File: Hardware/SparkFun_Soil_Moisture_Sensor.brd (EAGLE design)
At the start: 22.9 x 61 mm, 11 parts, among them Q1 2N3904

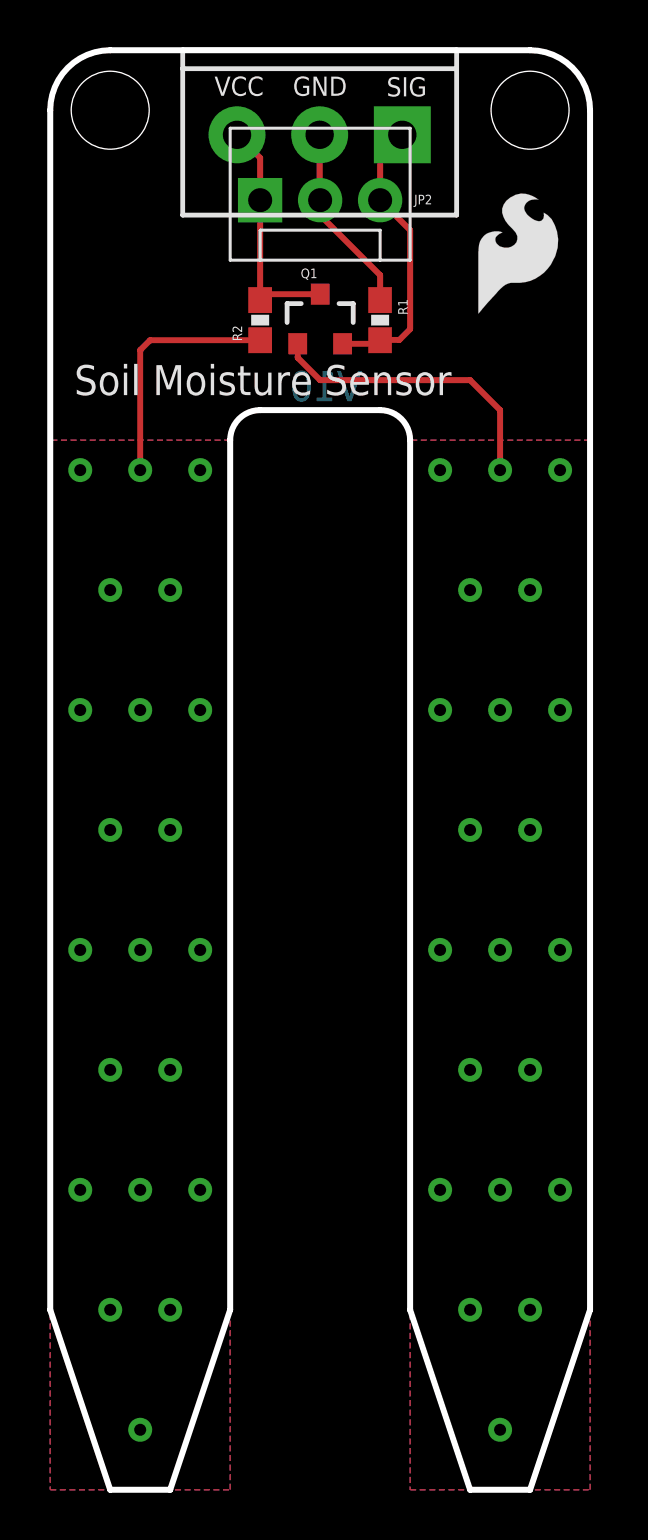
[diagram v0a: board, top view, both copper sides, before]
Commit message: Fixed QC Checklist issues
added fiducials, changed dimension width to .008, removed Ohm from
values, added Vcc range, changed version # to correct V01, corrected
dashed lines
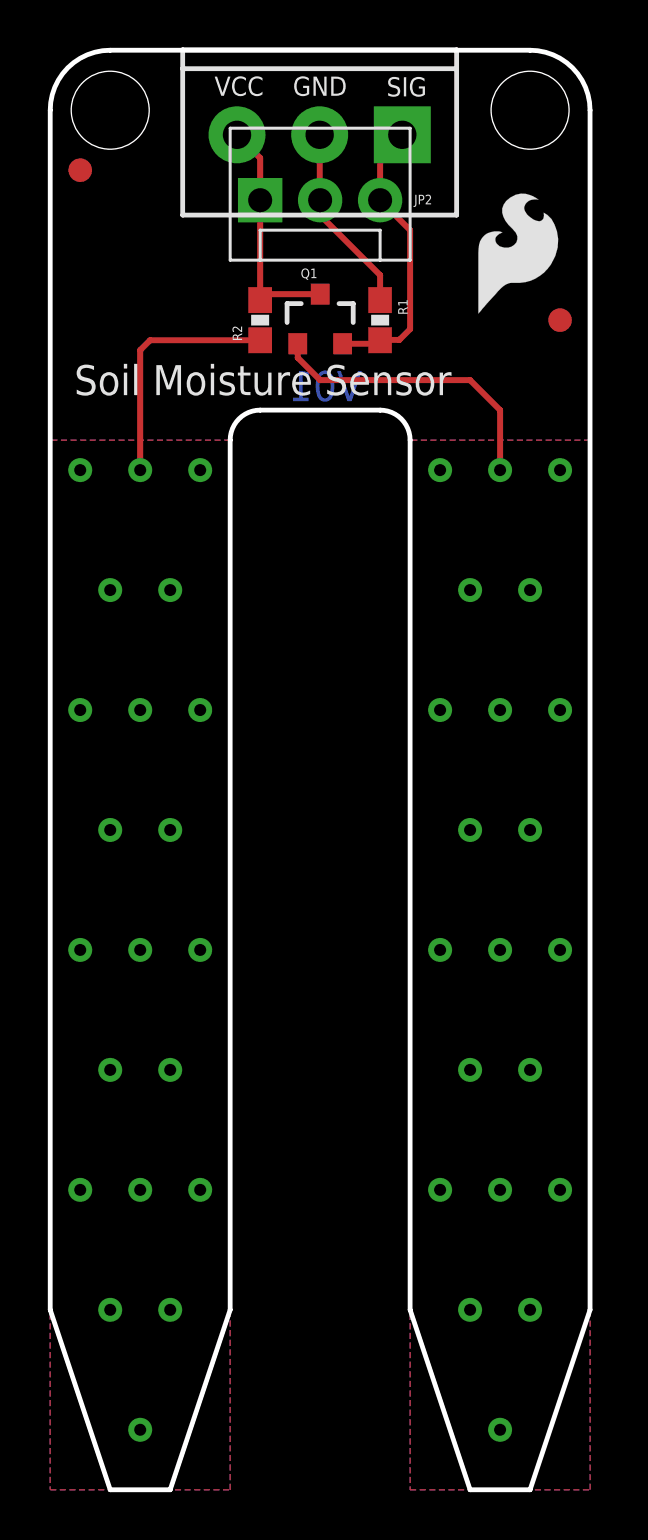
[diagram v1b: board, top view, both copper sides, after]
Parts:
- added FID1, FID2: FIDUCIAL1X2, SparkFun-Aesthetics:FIDUCIAL-1X2
- R1: value 10kOhm -> 10k
- R2: value 100Ohm -> 100
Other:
- board text added: "V01"
- board text removed: "V10"
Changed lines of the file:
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@@
 <grid distance="0.05" unitdist="inch" unit="inch" style="lines" multiple="1" display="yes" altdistance="0.005" altunitdist="inch" altunit="inch"/>
 <layers>
-<layer number="1" name="Top" color="4" fill="1" visible="no" active="yes"/>
+<layer number="1" name="Top" color="4" fill="1" visible="yes" active="yes"/>
 <layer number="2" name="Route2" color="1" fill="3" visible="no" active="no"/>
 <layer number="3" name="Route3" color="4" fill="3" visible="no" active="no"/>
@@
 <layer number="15" name="Route15" color="4" fill="6" visible="no" active="no"/>
 <layer number="16" name="Bottom" color="1" fill="1" visible="yes" active="yes"/>
-<layer number="17" name="Pads" color="2" fill="1" visible="no" active="yes"/>
-<layer number="18" name="Vias" color="2" fill="1" visible="no" active="yes"/>
-<layer number="19" name="Unrouted" color="6" fill="1" visible="no" active="yes"/>
-<layer number="20" name="Dimension" color="15" fill="1" visible="no" active="yes"/>
-<layer number="21" name="tPlace" color="16" fill="1" visible="no" active="yes"/>
-<layer number="22" name="bPlace" color="14" fill="1" visible="no" active="yes"/>
-<layer number="23" name="tOrigins" color="15" fill="1" visible="no" active="yes"/>
-<layer number="24" name="bOrigins" color="15" fill="1" visible="no" active="yes"/>
+<layer number="17" name="Pads" color="2" fill="1" visible="yes" active="yes"/>
+<layer number="18" name="Vias" color="2" fill="1" visible="yes" active="yes"/>
+<layer number="19" name="Unrouted" color="6" fill="1" visible="yes" active="yes"/>
+<layer number="20" name="Dimension" color="15" fill="1" visible="yes" active="yes"/>
+<layer number="21" name="tPlace" color="16" fill="1" visible="yes" active="yes"/>
+<layer number="22" name="bPlace" color="14" fill="1" visible="yes" active="yes"/>
+<layer number="23" name="tOrigins" color="15" fill="1" visible="yes" active="yes"/>
+<layer number="24" name="bOrigins" color="15" fill="1" visible="yes" active="yes"/>
 <layer number="25" name="tNames" color="7" fill="1" visible="no" active="yes"/>
 <layer number="26" name="bNames" color="7" fill="1" visible="no" active="yes"/>
 <layer number="27" name="tValues" color="7" fill="1" visible="no" active="yes"/>
 <layer number="28" name="bValues" color="7" fill="1" visible="no" active="yes"/>
-<layer number="29" name="tStop" color="7" fill="3" visible="yes" active="yes"/>
-<layer number="30" name="bStop" color="7" fill="6" visible="yes" active="yes"/>
+<layer number="29" name="tStop" color="7" fill="3" visible="no" active="yes"/>
+<layer number="30" name="bStop" color="7" fill="6" visible="no" active="yes"/>
 <layer number="31" name="tCream" color="7" fill="4" visible="no" active="yes"/>
 <layer number="32" name="bCream" color="7" fill="5" visible="no" active="yes"/>
@@
 <layer number="43" name="vRestrict" color="2" fill="10" visible="no" active="yes"/>
 <layer number="44" name="Drills" color="7" fill="1" visible="no" active="yes"/>
-<layer number="45" name="Holes" color="7" fill="1" visible="no" active="yes"/>
+<layer number="45" name="Holes" color="7" fill="1" visible="yes" active="yes"/>
 <layer number="46" name="Milling" color="3" fill="1" visible="no" active="yes"/>
 <layer number="47" name="Measures" color="7" fill="1" visible="no" active="yes"/>
@@
 <layer number="49" name="Reference" color="7" fill="1" visible="no" active="yes"/>
 <layer number="50" name="dxf" color="7" fill="1" visible="no" active="no"/>
-<layer number="51" name="tDocu" color="6" fill="1" visible="no" active="yes"/>
+<layer number="51" name="tDocu" color="6" fill="1" visible="yes" active="yes"/>
 <layer number="52" name="bDocu" color="7" fill="1" visible="no" active="yes"/>
 <layer number="53" name="tGND_GNDA" color="7" fill="9" visible="no" active="no"/>
@@
 <plain>
 <dimension x1="22.86" y1="60.96" x2="22.86" y2="0" x3="30.48" y3="30.48" textsize="1.778" textratio="15" layer="51" unit="inch"/>
-<wire x1="2.54" y1="60.96" x2="0" y2="58.42" width="0.254" layer="20" curve="90"/>
-<wire x1="0" y1="58.42" x2="0" y2="7.62" width="0.254" layer="20"/>
+<wire x1="2.54" y1="60.96" x2="0" y2="58.42" width="0.2032" layer="20" curve="90"/>
+<wire x1="0" y1="58.42" x2="0" y2="7.62" width="0.2032" layer="20"/>
 <dimension x1="0" y1="60.96" x2="22.86" y2="60.96" x3="11.43" y3="64.77" textsize="1.778" textratio="15" layer="51" unit="inch"/>
-<wire x1="2.54" y1="60.96" x2="20.32" y2="60.96" width="0.254" layer="20"/>
-<wire x1="20.32" y1="60.96" x2="22.86" y2="58.42" width="0.254" layer="20" curve="-90"/>
-<wire x1="22.86" y1="58.42" x2="22.86" y2="7.62" width="0.254" layer="20"/>
-<wire x1="22.86" y1="7.62" x2="20.32" y2="0" width="0.254" layer="20"/>
-<wire x1="20.32" y1="0" x2="17.78" y2="0" width="0.254" layer="20"/>
-<wire x1="17.78" y1="0" x2="15.24" y2="7.62" width="0.254" layer="20"/>
-<wire x1="0" y1="7.62" x2="2.54" y2="0" width="0.254" layer="20"/>
-<wire x1="2.54" y1="0" x2="5.08" y2="0" width="0.254" layer="20"/>
-<wire x1="5.08" y1="0" x2="7.62" y2="7.62" width="0.254" layer="20"/>
-<wire x1="7.62" y1="7.62" x2="7.62" y2="44.45" width="0.254" layer="20"/>
-<wire x1="7.62" y1="44.45" x2="8.89" y2="45.72" width="0.254" layer="20" curve="-90"/>
-<wire x1="8.89" y1="45.72" x2="13.97" y2="45.72" width="0.254" layer="20"/>
-<wire x1="15.24" y1="7.62" x2="15.24" y2="44.45" width="0.254" layer="20"/>
-<wire x1="15.24" y1="44.45" x2="13.97" y2="45.72" width="0.254" layer="20" curve="90"/>
+<wire x1="2.54" y1="60.96" x2="20.32" y2="60.96" width="0.2032" layer="20"/>
+<wire x1="20.32" y1="60.96" x2="22.86" y2="58.42" width="0.2032" layer="20" curve="-90"/>
+<wire x1="22.86" y1="58.42" x2="22.86" y2="7.62" width="0.2032" layer="20"/>
+<wire x1="22.86" y1="7.62" x2="20.32" y2="0" width="0.2032" layer="20"/>
+<wire x1="20.32" y1="0" x2="17.78" y2="0" width="0.2032" layer="20"/>
+<wire x1="17.78" y1="0" x2="15.24" y2="7.62" width="0.2032" layer="20"/>
+<wire x1="0" y1="7.62" x2="2.54" y2="0" width="0.2032" layer="20"/>
+<wire x1="2.54" y1="0" x2="5.08" y2="0" width="0.2032" layer="20"/>
+<wire x1="5.08" y1="0" x2="7.62" y2="7.62" width="0.2032" layer="20"/>
+<wire x1="7.62" y1="7.62" x2="7.62" y2="44.45" width="0.2032" layer="20"/>
+<wire x1="7.62" y1="44.45" x2="8.89" y2="45.72" width="0.2032" layer="20" curve="-90"/>
+<wire x1="8.89" y1="45.72" x2="13.97" y2="45.72" width="0.2032" layer="20"/>
+<wire x1="15.24" y1="7.62" x2="15.24" y2="44.45" width="0.2032" layer="20"/>
+<wire x1="15.24" y1="44.45" x2="13.97" y2="45.72" width="0.2032" layer="20" curve="90"/>
 <text x="12.573" y="59.8424" size="0.8128" layer="21" font="vector" ratio="15" rot="R180">GND</text>
 <text x="15.9512" y="59.817" size="0.8128" layer="21" font="vector" ratio="15" rot="R180">SIG</text>
@@
 <text x="12.7" y="59.563" size="1.016" layer="22" font="vector" ratio="15" rot="SMR0">GND</text>
 <text x="19.05" y="-10.16" size="1.778" layer="51" font="vector" ratio="10">Joel Bartlett</text>
-<text x="13.208" y="46.101" size="1.27" layer="16" font="vector" ratio="15" rot="SMR0">V10</text>
+<text x="13.208" y="46.101" size="1.27" layer="16" font="vector" ratio="15" rot="SMR0">V01</text>
 <dimension x1="7.62" y1="7.62" x2="15.24" y2="7.62" x3="11.43" y3="1.27" textsize="1.27" textratio="15" layer="51" unit="inch"/>
 <dimension x1="2.54" y1="58.42" x2="20.32" y2="58.42" x3="11.43" y3="62.23" textsize="1.27" textratio="15" layer="51" unit="inch"/>
@@
 <attribute name="PROD_ID" value="TRANS-08049" x="11.43" y="49.53" size="1.778" layer="27" font="vector" ratio="15" display="off"/>
 </element>
-<element name="R1" library="SparkFun-Resistors" package="0603-RES" value="10kOhm" x="13.97" y="49.53" rot="R270">
+<element name="R1" library="SparkFun-Resistors" package="0603-RES" value="10k" x="13.97" y="49.53" rot="R270">
 <attribute name="PROD_ID" value="RES-12438" x="13.97" y="49.53" size="1.778" layer="27" font="vector" ratio="15" rot="R270" display="off"/>
 </element>
-<element name="R2" library="SparkFun-Resistors" package="0603-RES" value="100Ohm" x="8.89" y="49.53" rot="R90">
+<element name="R2" library="SparkFun-Resistors" package="0603-RES" value="100" x="8.89" y="49.53" rot="R90">
 <attribute name="PROD_ID" value="RES-12438" x="8.89" y="49.53" size="1.778" layer="27" font="vector" ratio="15" rot="R90" display="off"/>
 </element>
@@
 <element name="STANDOFF1" library="SparkFun-Electromechanical" package="STAND-OFF" value="STAND-OFF" x="2.54" y="58.42"/>
 <element name="STANDOFF2" library="SparkFun-Electromechanical" package="STAND-OFF" value="STAND-OFF" x="20.32" y="58.42"/>
+<element name="FID1" library="SparkFun-Aesthetics" package="FIDUCIAL-1X2" value="FIDUCIAL1X2" x="1.27" y="55.88"/>
+<element name="FID2" library="SparkFun-Aesthetics" package="FIDUCIAL-1X2" value="FIDUCIAL1X2" x="21.59" y="49.53"/>
 </elements>
 <signals>
@@
 </polygon>
 <via x="19.05" y="43.18" extent="1-16" drill="0.508"/>
-<polygon width="0.254" layer="16" isolate="0.3048">
+<polygon width="0.2032" layer="16" isolate="0.3048">
 <vertex x="15.24" y="44.45"/>
 <vertex x="15.24" y="0"/>
